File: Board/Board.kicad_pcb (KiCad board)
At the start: 2 copper layers, 69.9 x 58.4 mm, 57 parts, among them J1 Screw_Terminal_1x02, P1 USB_B, P2 CONN_01X05, P3 CONN_01X06, SW1 SW_SPST, SW2 SW_SPST, U1 MCP23016, U2 LM1117-3.3, U3 MCP9808, U4 ESP-12E

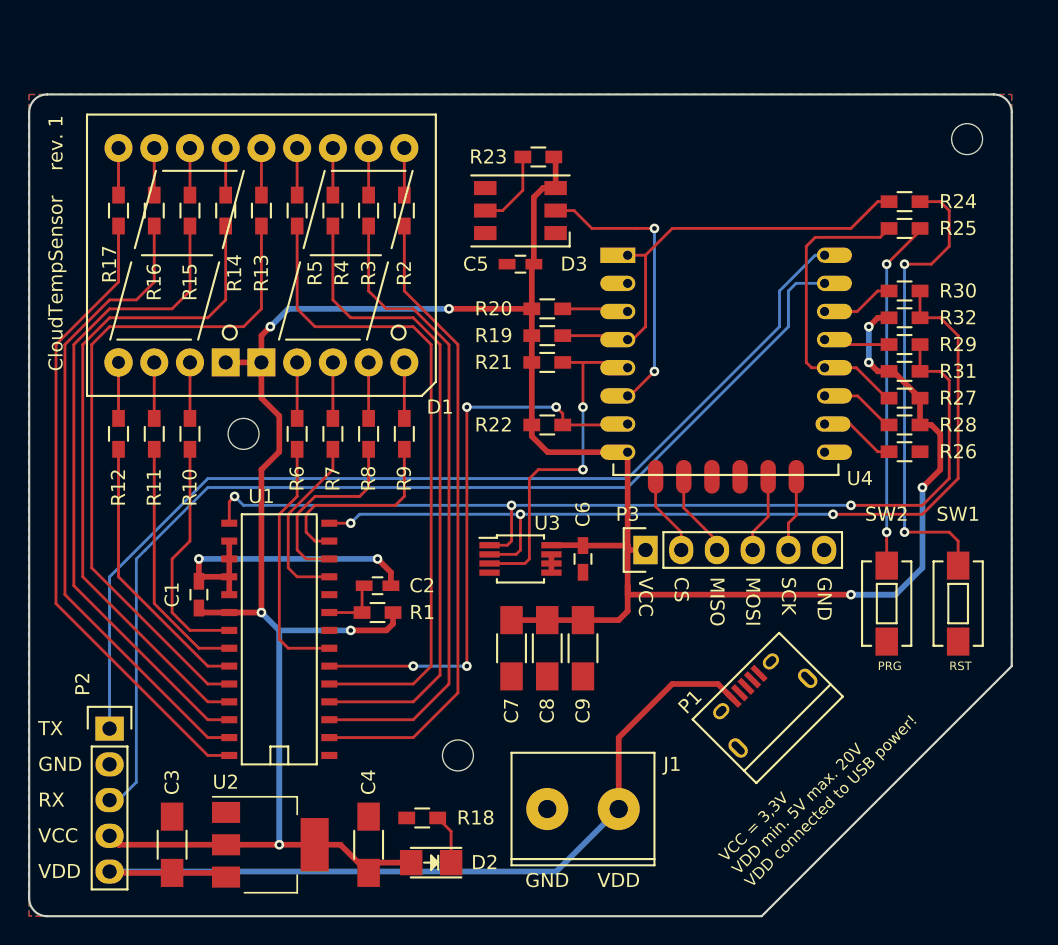
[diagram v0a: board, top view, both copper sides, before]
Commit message: Fix footprint for U1
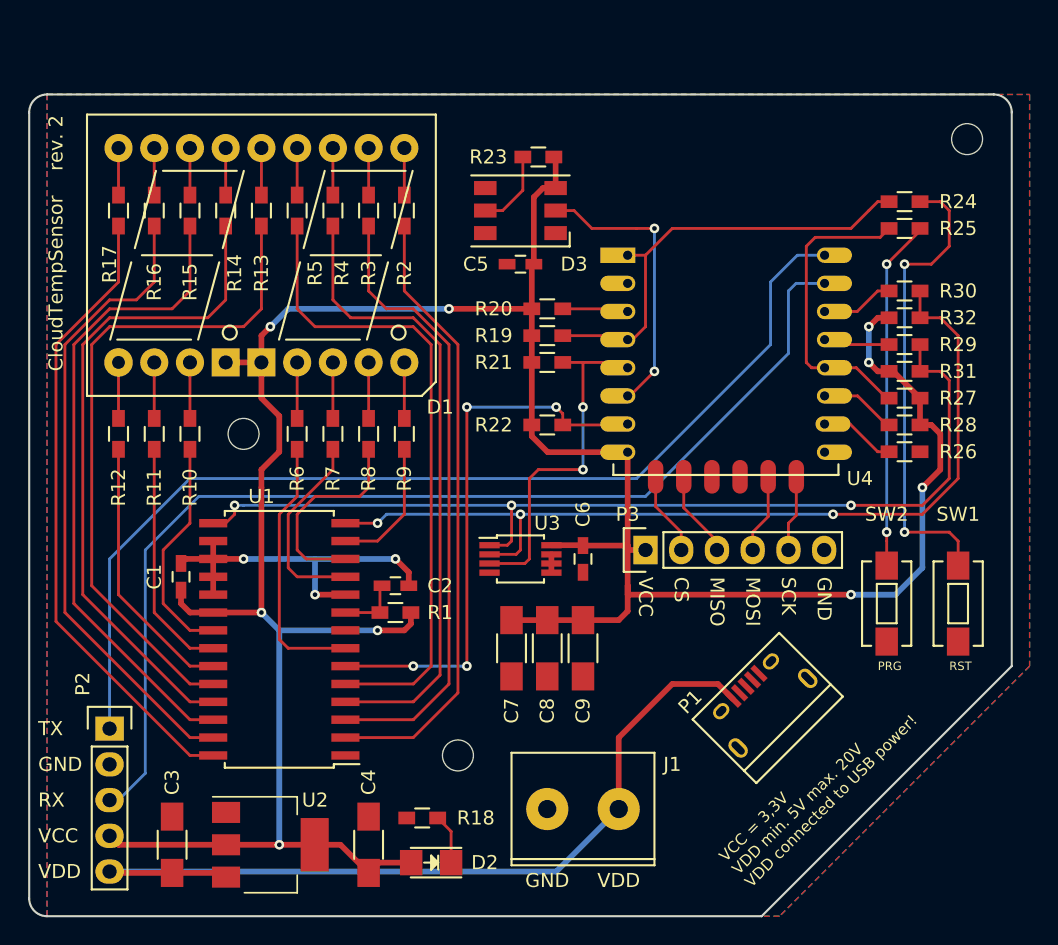
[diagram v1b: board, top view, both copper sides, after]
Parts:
- U1: footprint SMD_Packages:SOIC-28 -> Housings_SOIC:SOIC-28W_7.5x17.9mm_Pitch1.27mm
- moved C1 1.80 mm to (87.6, 97.8)
- moved C2 1.27 mm to (102.9, 98.4)
- moved R1 1.27 mm to (102.9, 100.3)
- turned U1 to 180 degrees
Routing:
- net Net-(R9-Pad2): track 14.0 -> 9.59 mm
- net GND: track 24.0 -> 28.4 mm, vias 2 -> 3
- net VCC: track 197.4 -> 201.0 mm
- net TX: track 72.6 -> 74.4 mm
- net SCL: track 66.2 -> 65.0 mm
- net Net-(R8-Pad2): track 13.7 -> 14.8 mm
- net Net-(R7-Pad2): track 12.9 -> 14.1 mm
- net Net-(R6-Pad2): track 17.9 -> 19.0 mm
- net Net-(R5-Pad2): track 47.1 -> 45.9 mm
- net Net-(R4-Pad2): track 46.3 -> 45.2 mm
- net Net-(R3-Pad2): track 45.6 -> 44.5 mm
- net Net-(R2-Pad2): track 45.2 -> 44.1 mm
- net IOINT: track 41.0 -> 39.9 mm
- net RX: track 76.8 -> 77.9 mm
- net Net-(R11-Pad2): track 17.6 -> 17.1 mm
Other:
- board text added: "CloudTempSensor rev. 2"
- board text removed: "CloudTempSensor rev. 1"

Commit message: Board Revision 3: Thermal relief for the temp sensor
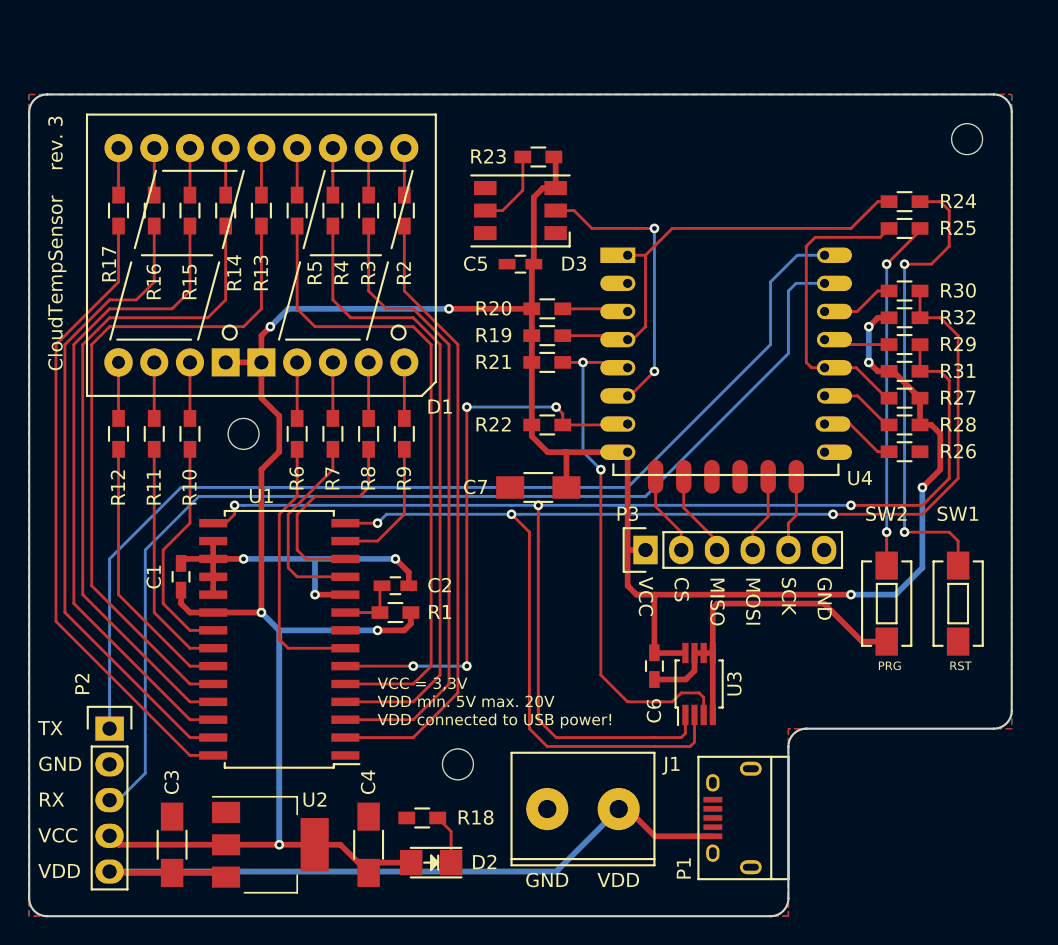
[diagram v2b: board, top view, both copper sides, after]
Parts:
- removed C8, C9: 22µ, Capacitors_SMD:C_1206_HandSoldering
- removed the REF** at (92.1, 87.6)
- removed the REF** at (143.5, 66.7)
- removed the REF** at (107.3, 110.5)
- added REF**: MountingHole_2.2mm_M2, Mounting_Holes:MountingHole_2.2mm_M2, F.Cu at (92.1, 87.6)
- added REF**: MountingHole_2.2mm_M2, Mounting_Holes:MountingHole_2.2mm_M2, F.Cu at (143.5, 66.7)
- added REF**: MountingHole_2.2mm_M2, Mounting_Holes:MountingHole_2.2mm_M2, F.Cu at (107.3, 111.1)
- moved U3 15.5 mm to (124.5, 105.4), turned to 90 degrees
- moved C7 11.6 mm to (113.0, 91.4), turned to 180 degrees
- moved C6 9.16 mm to (121.3, 104.1)
- moved P1 8.47 mm to (127.0, 114.9), turned to 90 degrees
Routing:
- net GND: track 28.4 -> 54.0 mm
- net SCL: track 65.0 -> 90.3 mm
- net SDA: track 69.5 -> 92.9 mm
- net Alert: track 25.7 -> 37.8 mm
- net VCC: track 201.0 -> 193.2 mm
- net VDD: track 61.9 -> 54.1 mm
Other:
- outline, holes or cut-outs redrawn
- board text added: "CloudTempSensor rev. 3"
- board text removed: "CloudTempSensor rev. 2"

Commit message: I2C connector and more thermal decoupling
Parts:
- added P4: CONN_01X03, Pin_Headers:Pin_Header_Straight_1x03, F.Cu at (114.9, 95.9)
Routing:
- net SCL: track 90.3 -> 92.8 mm
- net SDA: track 92.9 -> 94.8 mm
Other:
- board text added: "SCL"
- board text added: "SDA"
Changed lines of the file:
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@@
 (kicad_pcb (version 4) (host pcbnew 4.0.5+dfsg1-4)
   (general
-    (links 121)
+    (links 124)
     (no_connects 0)
     (area 76.759999 63.424999 146.760001 121.995001)
     (thickness 1.6)
-    (drawings 30)
-    (tracks 408)
+    (drawings 33)
+    (tracks 412)
     (zones 0)
-    (modules 55)
+    (modules 56)
     (nets 67)
   )
@@
     (fp_circle (center 0 0) (end 2.45 0) (layer F.CrtYd) (width 0.05))
     (pad 1 np_thru_hole circle (at 0 0) (size 2.2 2.2) (drill 2.2) (layers *.Cu *.Mask))
+  )
+  (module Pin_Headers:Pin_Header_Straight_1x03 (layer F.Cu)
+    (at 114.935 95.885)
+    (descr "Through hole pin header")
+    (tags "pin header")
+    (fp_text reference P4 (at 0 7.62) (layer F.SilkS)
+      (effects (font (size 1 1) (thickness 0.15)))
+    )
+    (fp_text value CONN_01X03 (at 0 -3.1) (layer F.Fab)
+      (effects (font (size 1 1) (thickness 0.15)))
+    )
+    (fp_line (start -1.75 -1.75) (end -1.75 6.85) (layer F.CrtYd) (width 0.05))
+    (fp_line (start 1.75 -1.75) (end 1.75 6.85) (layer F.CrtYd) (width 0.05))
+    (fp_line (start -1.75 -1.75) (end 1.75 -1.75) (layer F.CrtYd) (width 0.05))
+    (fp_line (start -1.75 6.85) (end 1.75 6.85) (layer F.CrtYd) (width 0.05))
+    (fp_line (start -1.27 1.27) (end -1.27 6.35) (layer F.SilkS) (width 0.15))
+    (fp_line (start -1.27 6.35) (end 1.27 6.35) (layer F.SilkS) (width 0.15))
+    (fp_line (start 1.27 6.35) (end 1.27 1.27) (layer F.SilkS) (width 0.15))
+    (fp_line (start 1.55 -1.55) (end 1.55 0) (layer F.SilkS) (width 0.15))
+    (fp_line (start 1.27 1.27) (end -1.27 1.27) (layer F.SilkS) (width 0.15))
+    (fp_line (start -1.55 0) (end -1.55 -1.55) (layer F.SilkS) (width 0.15))
+    (fp_line (start -1.55 -1.55) (end 1.55 -1.55) (layer F.SilkS) (width 0.15))
+    (pad 1 thru_hole rect (at 0 0) (size 2.032 1.7272) (drill 1.016) (layers *.Cu *.Mask)
+      (net 54 SCL))
+    (pad 2 thru_hole oval (at 0 2.54) (size 2.032 1.7272) (drill 1.016) (layers *.Cu *.Mask)
+      (net 2 GND))
+    (pad 3 thru_hole oval (at 0 5.08) (size 2.032 1.7272) (drill 1.016) (layers *.Cu *.Mask)
+      (net 55 SDA))
+    (model Pin_Headers.3dshapes/Pin_Header_Straight_1x03.wrl
+      (at (xyz 0 -0.1 0))
+      (scale (xyz 1 1 1))
+      (rotate (xyz 0 0 90))
+    )
+  )
+  (gr_text SDA (at 109.855 100.965) (layer F.SilkS)
+    (effects (font (size 1 1) (thickness 0.1)) (justify left))
+  )
+  (gr_text SCL (at 109.855 95.885) (layer F.SilkS)
+    (effects (font (size 1 1) (thickness 0.1)) (justify left))
+  )
+  (gr_text GND (at 109.855 98.425) (layer F.SilkS)
+    (effects (font (size 1 1) (thickness 0.1)) (justify left))
   )
   (gr_line (start 146.685 107.315) (end 146.685 64.77) (angle 90) (layer Edge.Cuts) (width 0.15))
@@
   (segment (start 137.795 86.995) (end 135.73 84.93) (width 0.2032) (layer F.Cu) (net 53))
   (segment (start 135.73 84.93) (end 133.38 84.93) (width 0.2032) (layer F.Cu) (net 53))
+  (segment (start 114.935 95.885) (end 114.935 93.345) (width 0.2032) (layer B.Cu) (net 54))
   (segment (start 124.135 107.61) (end 124.135 109.545) (width 0.2032) (layer F.Cu) (net 54))
   (segment (start 121.285 109.855) (end 113.665 109.855) (width 0.2032) (layer F.Cu) (net 54))
@@
   (segment (start 133.985 93.345) (end 140.335 93.345) (width 0.2032) (layer F.Cu) (net 54))
   (via (at 133.985 93.345) (size 0.6858) (drill 0.3302) (layers F.Cu B.Cu) (net 54))
-  (segment (start 111.76 93.345) (end 133.985 93.345) (width 0.2032) (layer B.Cu) (net 54))
+  (segment (start 111.76 93.345) (end 114.935 93.345) (width 0.2032) (layer B.Cu) (net 54))
+  (segment (start 114.935 93.345) (end 133.985 93.345) (width 0.2032) (layer B.Cu) (net 54))
   (segment (start 140.165 79.375) (end 140.165 77.47) (width 0.2032) (layer F.Cu) (net 54))
+  (segment (start 114.935 100.965) (end 113.03 100.965) (width 0.2032) (layer F.Cu) (net 55))
   (segment (start 123.485 107.61) (end 123.485 108.925) (width 0.2032) (layer F.Cu) (net 55))
   (segment (start 121.285 109.22) (end 114.3 109.22) (width 0.2032) (layer F.Cu) (net 55))
@@
   (via (at 113.03 92.71) (size 0.6858) (drill 0.3302) (layers F.Cu B.Cu) (net 55))
   (segment (start 114.3 109.22) (end 114.3 109.22) (width 0.2032) (layer F.Cu) (net 55))
-  (segment (start 113.03 107.95) (end 113.03 95.25) (width 0.2032) (layer F.Cu) (net 55))
+  (segment (start 113.03 107.95) (end 113.03 100.965) (width 0.2032) (layer F.Cu) (net 55))
+  (segment (start 113.03 100.965) (end 113.03 95.25) (width 0.2032) (layer F.Cu) (net 55))
   (segment (start 114.3 109.22) (end 113.03 107.95) (width 0.2032) (layer F.Cu) (net 55))
   (segment (start 91.44 92.71) (end 91.44 93.345) (width 0.2032) (layer F.Cu) (net 55))
@@
     (polygon
       (pts
-        (xy 128.905 110.49) (xy 119.38 110.49) (xy 119.38 100.33) (xy 128.905 100.33)
+        (xy 128.905 110.49) (xy 119.38 110.49) (xy 119.38 99.695) (xy 128.905 99.695)
       )
     )
@@
     (polygon
       (pts
-        (xy 128.905 110.49) (xy 119.38 110.49) (xy 119.38 100.33) (xy 128.905 100.33)
+        (xy 128.905 110.49) (xy 119.38 110.49) (xy 119.38 99.695) (xy 128.905 99.695)
       )
     )
+  )
+  (zone (net 0) (net_name "") (layer B.Cu) (hatch edge 0.508)
+    (connect_pads (clearance 0.254))
+    (min_thickness 0.254)
+    (keepout (tracks allowed) (vias allowed) (copperpour not_allowed))
+    (fill (arc_segments 16) (thermal_gap 0.508) (thermal_bridge_width 0.508))
+    (polygon
+      (pts
+        (xy 116.205 89.535) (xy 114.935 89.535) (xy 114.935 66.04) (xy 116.205 66.04)
+      )
+    )
+  )
+  (zone (net 0) (net_name "") (layer F.Cu) (hatch edge 0.508)
+    (connect_pads (clearance 0.254))
+    (min_thickness 0.254)
+    (keepout (tracks allowed) (vias allowed) (copperpour not_allowed))
+    (fill (arc_segments 16) (thermal_gap 0.508) (thermal_bridge_width 0.508))
+    (polygon
+      (pts
+        (xy 116.205 89.535) (xy 114.935 89.535) (xy 114.935 66.04) (xy 116.205 66.04)
+      )
+    )
+  )
+  (zone (net 0) (net_name "") (layer F.Cu) (hatch edge 0.508)
+    (connect_pads (clearance 0.254))
+    (min_thickness 0.254)
+    (keepout (tracks allowed) (vias allowed) (copperpour not_allowed))
+    (fill (arc_segments 16) (thermal_gap 0.508) (thermal_bridge_width 0.508))
+    (polygon
+      (pts
+        (xy 116.205 102.87) (xy 116.205 120.015) (xy 114.935 120.015) (xy 114.935 102.87)
+      )
+    )
+  )
+  (zone (net 0) (net_name "") (layer B.Cu) (hatch edge 0.508)
+    (connect_pads (clearance 0.254))
+    (min_thickness 0.254)
+    (keepout (tracks allowed) (vias allowed) (copperpour not_allowed))
+    (fill (arc_segments 16) (thermal_gap 0.508) (thermal_bridge_width 0.508))
+    (polygon
+      (pts
+        (xy 116.205 102.87) (xy 116.205 120.015) (xy 114.935 120.015) (xy 114.935 102.87)
+      )
+    )
